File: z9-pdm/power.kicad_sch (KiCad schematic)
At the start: 18 parts, among them Q2 DMT6007LFG, U3 LM74700, U4 VN9016AJTR

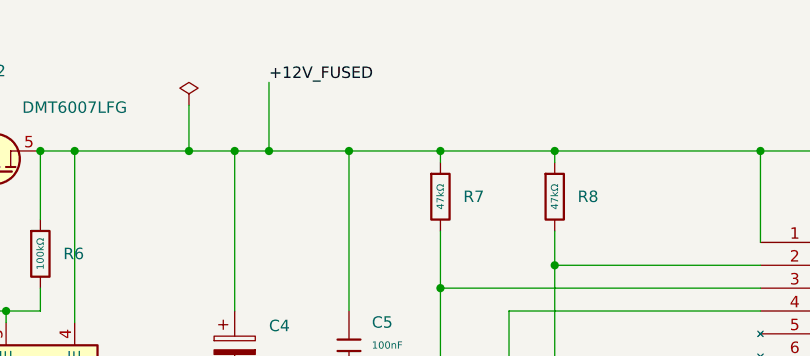
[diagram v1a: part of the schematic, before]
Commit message: z9-pdm: rename 12V net label and add wire connections
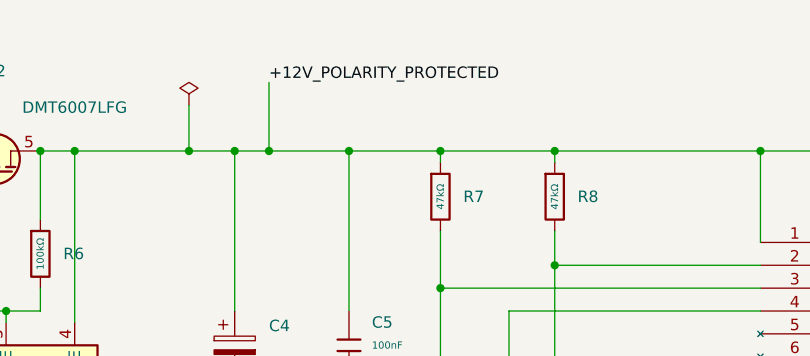
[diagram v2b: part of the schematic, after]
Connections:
- net +12V_FUSED renamed +12V_POLARITY_PROTECTED
